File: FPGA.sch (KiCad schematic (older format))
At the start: 14 parts, among them U13 ADS1015, U14 SiT8008B, U8 GW1N-9LQ100

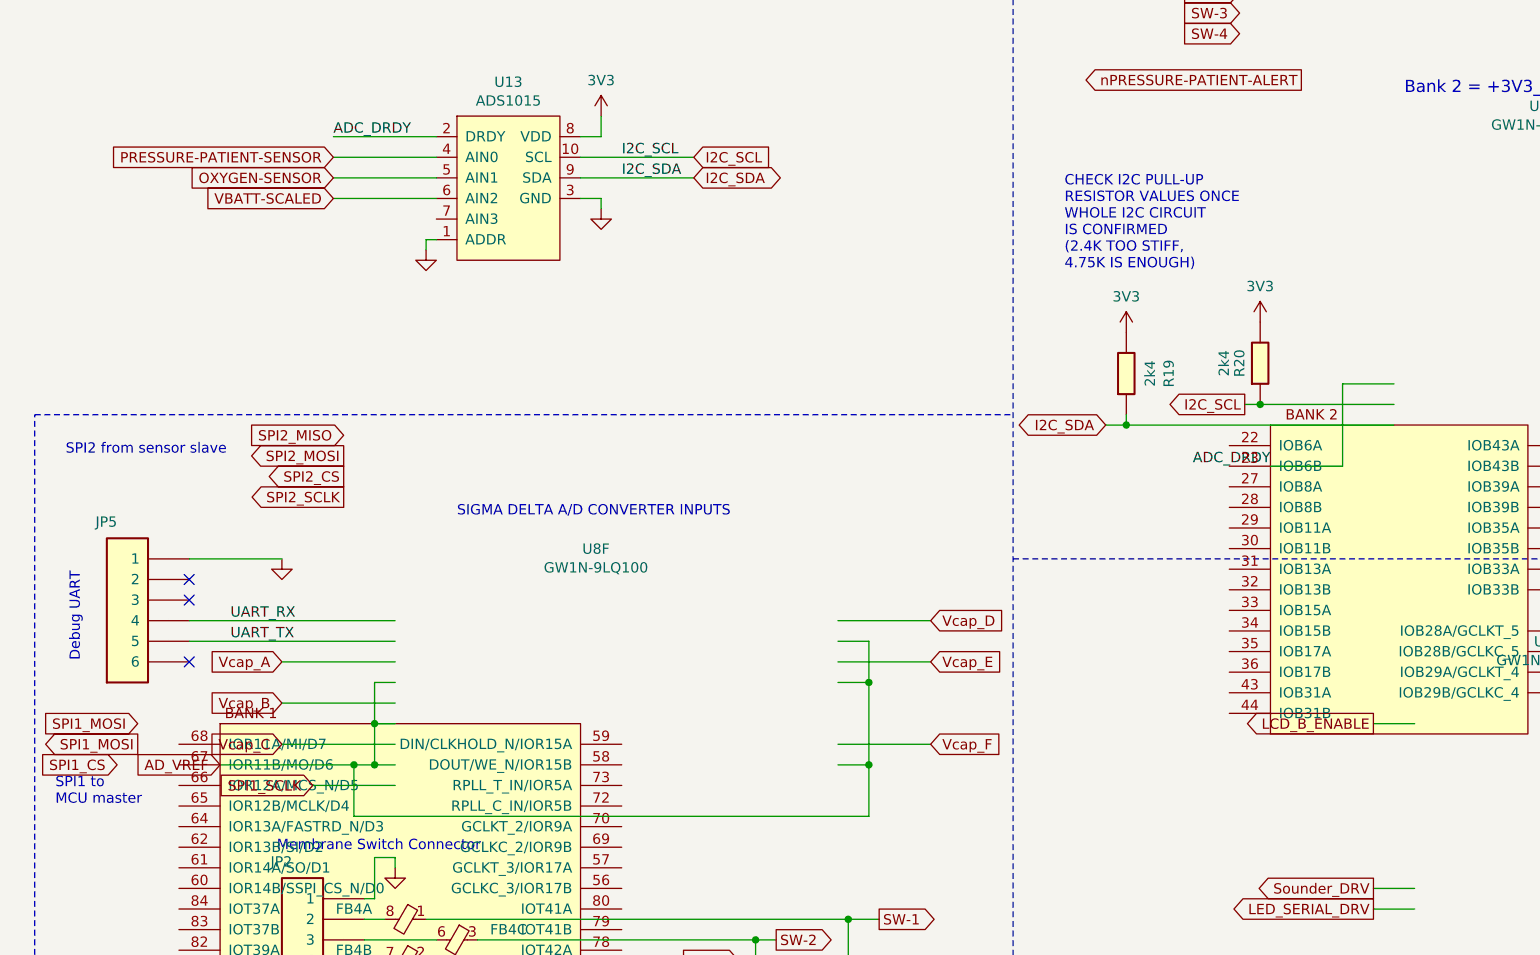
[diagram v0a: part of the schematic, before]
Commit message: SPI from FPGA to MCU and pressure sensor pins changed
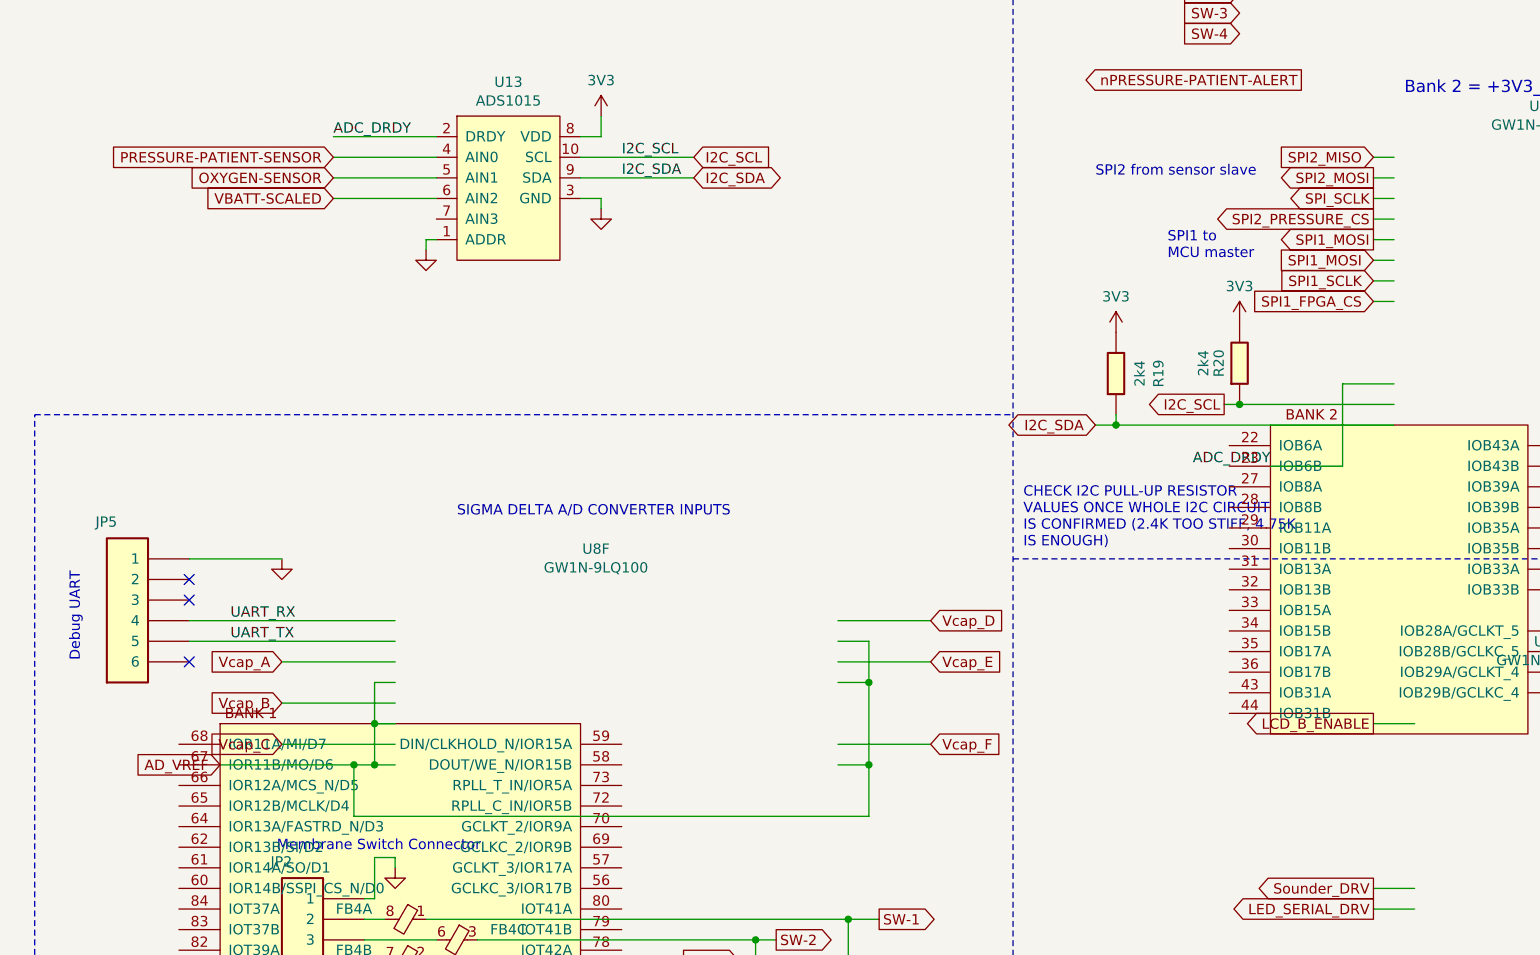
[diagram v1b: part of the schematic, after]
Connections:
- net labels added: SPI1_FPGA_CS, SPI2_PRESSURE_CS, SPI_SCLK
- net labels removed: SPI1_CS, SPI2_CS, SPI2_SCLK
- wire segments 105 -> 112
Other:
- note added: "CHECK I2C PULL-UP RESISTOR\nVALUES ONCE WHOLE I2C CIRCUIT\nIS CONFIRMED (2.4K TOO STIFF, 4.75K\nIS ENOUGH)"
- note removed: "CHECK I2C PULL-UP\nRESISTOR VALUES ONCE\nWHOLE I2C CIRCUIT\nIS CONFIRMED\n(2.4K TOO STIFF,\n4.75K IS ENOUGH)"
- moved on the sheet: R19, R20
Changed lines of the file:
@@
 L OpenVent:2k4_0603_Chip_Resistor,_1%,_0.1W R19
 U 1 1 5FD4D09C
-P 5700 2650
-F 0 "R19" H 5800 2343 50  0000 C CNN
-F 1 "2k4_0603_Chip_Resistor,_1%,_0.1W" H 5700 2650 50  0001 C CNN
-F 2 "Resistor_SMD:R_0603_1608Metric" H 5700 2650 50  0001 C CNN
-F 3 "" H 5700 2650 50  0001 C CNN
-F 4 "2k4" H 5800 2434 50  0000 C CNN "Val"
-F 5 "1%" H 5700 2650 50  0001 C CNN "Tolerance"
-F 6 "0.1W" H 5700 2650 50  0001 C CNN "Watt"
-	1    5700 2650
+P 5650 2650
+F 0 "R19" H 5750 2343 50  0000 C CNN
+F 1 "2k4_0603_Chip_Resistor,_1%,_0.1W" H 5650 2650 50  0001 C CNN
+F 2 "Resistor_SMD:R_0603_1608Metric" H 5650 2650 50  0001 C CNN
+F 3 "" H 5650 2650 50  0001 C CNN
+F 4 "2k4" H 5750 2434 50  0000 C CNN "Val"
+F 5 "1%" H 5650 2650 50  0001 C CNN "Tolerance"
+F 6 "0.1W" H 5650 2650 50  0001 C CNN "Watt"
+	1    5650 2650
 	0    -1   -1   0
 $EndComp
@@
 L OpenVent:2k4_0603_Chip_Resistor,_1%,_0.1W R20
 U 1 1 5FD4E271
-P 6350 2600
-F 0 "R20" H 6450 2600 50  0000 C CNN
-F 1 "2k4_0603_Chip_Resistor,_1%,_0.1W" H 6350 2600 50  0001 C CNN
-F 2 "Resistor_SMD:R_0603_1608Metric" H 6350 2600 50  0001 C CNN
-F 3 "" H 6350 2600 50  0001 C CNN
-F 4 "2k4" H 6450 2675 50  0000 C CNN "Val"
-F 5 "1%" H 6350 2600 50  0001 C CNN "Tolerance"
-F 6 "0.1W" H 6350 2600 50  0001 C CNN "Watt"
-	1    6350 2600
+P 6250 2600
+F 0 "R20" H 6350 2600 50  0000 C CNN
+F 1 "2k4_0603_Chip_Resistor,_1%,_0.1W" H 6250 2600 50  0001 C CNN
+F 2 "Resistor_SMD:R_0603_1608Metric" H 6250 2600 50  0001 C CNN
+F 3 "" H 6250 2600 50  0001 C CNN
+F 4 "2k4" H 6350 2675 50  0000 C CNN "Val"
+F 5 "1%" H 6250 2600 50  0001 C CNN "Tolerance"
+F 6 "0.1W" H 6250 2600 50  0001 C CNN "Watt"
+	1    6250 2600
 	0    -1   -1   0
 $EndComp
@@
 L OpenVent:3V3 #PWR031
 U 1 1 5FD519F4
-P 5800 2350
-F 0 "#PWR031" H 5800 2200 50  0001 C CNN
-F 1 "3V3" H 5800 2523 50  0000 C CNN
-F 2 "" H 5800 2350 50  0001 C CNN
-F 3 "" H 5800 2350 50  0001 C CNN
-	1    5800 2350
+P 5750 2350
+F 0 "#PWR031" H 5750 2200 50  0001 C CNN
+F 1 "3V3" H 5750 2523 50  0000 C CNN
+F 2 "" H 5750 2350 50  0001 C CNN
+F 3 "" H 5750 2350 50  0001 C CNN
+	1    5750 2350
 	1    0    0    -1
 $EndComp
@@
 Wire Notes Line
 	500  7750 500  2750
-Text Notes 5500 2050 0    50   ~ 0
-CHECK I2C PULL-UP\nRESISTOR VALUES ONCE\nWHOLE I2C CIRCUIT\nIS CONFIRMED\n(2.4K TOO STIFF,\n4.75K IS ENOUGH)
-Text GLabel 6375 2700 0    50   Output ~ 0
+Text Notes 5300 3400 0    50   ~ 0
+CHECK I2C PULL-UP RESISTOR\nVALUES ONCE WHOLE I2C CIRCUIT\nIS CONFIRMED (2.4K TOO STIFF, 4.75K\nIS ENOUGH)
+Text GLabel 6275 2700 0    50   Output ~ 0
 I2C_SCL
-Text GLabel 5700 2800 0    50   BiDi ~ 0
+Text GLabel 5650 2800 0    50   BiDi ~ 0
 I2C_SDA
 Text GLabel 3700 1500 2    50   Input ~ 0
@@
 I2C_SDA
 Wire Wire Line
-	6375 2700 6450 2700
+	6275 2700 6350 2700
 $Comp
 L OpenVent:3V3 #PWR066
 U 1 1 602573F8
-P 6450 2300
-F 0 "#PWR066" H 6450 2150 50  0001 C CNN
-F 1 "3V3" H 6450 2473 50  0000 C CNN
-F 2 "" H 6450 2300 50  0001 C CNN
-F 3 "" H 6450 2300 50  0001 C CNN
-	1    6450 2300
+P 6350 2300
+F 0 "#PWR066" H 6350 2150 50  0001 C CNN
+F 1 "3V3" H 6350 2473 50  0000 C CNN
+F 2 "" H 6350 2300 50  0001 C CNN
+F 3 "" H 6350 2300 50  0001 C CNN
+	1    6350 2300
 	1    0    0    -1
 $EndComp
@@
 Text Notes 2550 3250 0    50   ~ 0
 SIGMA DELTA A/D CONVERTER INPUTS
-Wire Wire Line
-	7100 2700 6450 2700
-Connection ~ 6450 2700
-Wire Wire Line
-	5700 2800 5800 2800
-Wire Wire Line
-	5800 2750 5800 2800
-Connection ~ 5800 2800
-Wire Wire Line
-	5800 2800 7100 2800
+Connection ~ 6350 2700
 Wire Wire Line
 	9000 2400 9000 3000
@@
 Wire Notes Line
 	500  2750 5250 2750
-Text GLabel 1850 4550 0    50   Input ~ 0
+Text GLabel 7000 2100 0    50   Input ~ 0
 SPI1_SCLK
-Wire Wire Line
-	1850 4550 2250 4550
-Text GLabel 900  4450 0    50   Input ~ 0
-SPI1_CS
-Text GLabel 1000 4250 0    50   Input ~ 0
+Text GLabel 7000 2200 0    50   Input ~ 0
+SPI1_FPGA_CS
+Text GLabel 7000 2000 0    50   Input ~ 0
 SPI1_MOSI
-Text GLabel 1000 4350 0    50   Output ~ 0
+Text GLabel 7000 1900 0    50   Output ~ 0
 SPI1_MOSI
 Wire Wire Line
@@
 Wire Wire Line
 	4550 4450 4550 4700
-Text GLabel 2000 2950 0    50   Output ~ 0
+Text GLabel 7000 1600 0    50   Output ~ 0
 SPI2_MOSI
-Text GLabel 2000 2850 0    50   Input ~ 0
+Text GLabel 7000 1500 0    50   Input ~ 0
 SPI2_MISO
-Text GLabel 2000 3050 0    50   Output ~ 0
-SPI2_CS
-Text GLabel 2000 3150 0    50   Output ~ 0
-SPI2_SCLK
-Text Notes 600  4650 0    50   ~ 0
+Text GLabel 7000 1800 0    50   Output ~ 0
+SPI2_PRESSURE_CS
+Text GLabel 7000 1700 0    50   Output ~ 0
+SPI_SCLK
+Text Notes 6000 2000 0    50   ~ 0
 SPI1 to\nMCU master
-Text Notes 650  2950 0    50   ~ 0
+Text Notes 5650 1600 0    50   ~ 0
 SPI2 from sensor slave
+Wire Wire Line
+	5750 2750 5750 2800
+Connection ~ 5750 2800
+Wire Wire Line
+	5750 2800 5650 2800
+Wire Wire Line
+	7100 1500 7000 1500
+Wire Wire Line
+	7100 1600 7000 1600
+Wire Wire Line
+	7100 1800 7000 1800
+Wire Wire Line
+	7000 1700 7100 1700
+Wire Wire Line
+	6350 2700 7100 2700
+Wire Wire Line
+	5750 2800 7100 2800
+Wire Wire Line
+	7100 1900 7000 1900
+Wire Wire Line
+	7100 2000 7000 2000
+Wire Wire Line
+	7100 2100 7000 2100
+Wire Wire Line
+	7100 2200 7000 2200
 $EndSCHEMATC

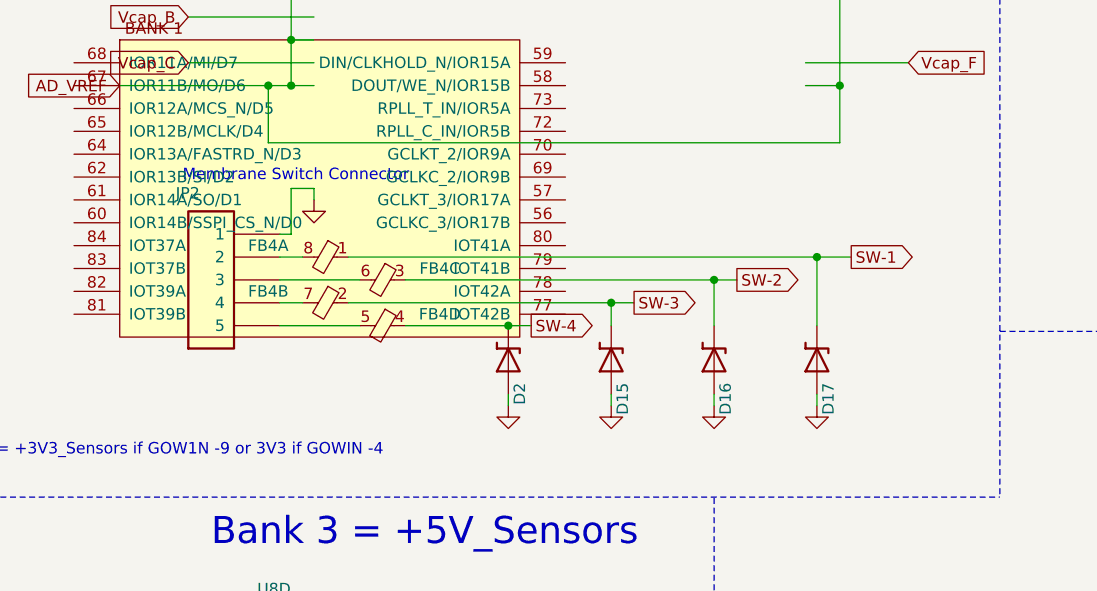
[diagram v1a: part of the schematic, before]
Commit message: Push buttons moved from FPGA pg 6 to UI pg 8
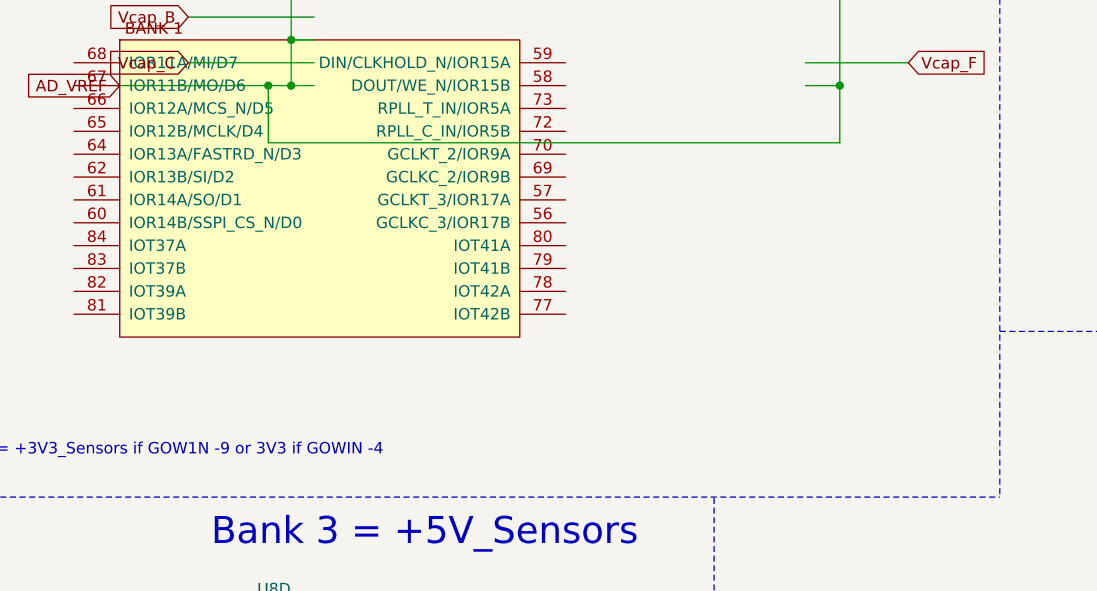
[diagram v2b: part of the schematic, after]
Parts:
- removed D15, D16, D17, D2: SP3522-01UTG, 0603 diode, symbol OpenVent:SP3522-01UTG
- removed FB4: BLA31BD121SN4D, F_Inductors:Murata_BLA31, symbol OpenVent:BLA31BD121SN4D
- removed JP2: Pin_Header,_1x5-Way,_2.54mm_Pitch, Connector_PinHeader_2.54mm:PinHeader_1x05_P2.54mm_Vertical, symbol OpenVent:Pin_Header,_1x5-Way,_2.54mm_Pitch
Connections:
- wire segments 112 -> 89
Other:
- note removed: "Membrane Switch Connector"

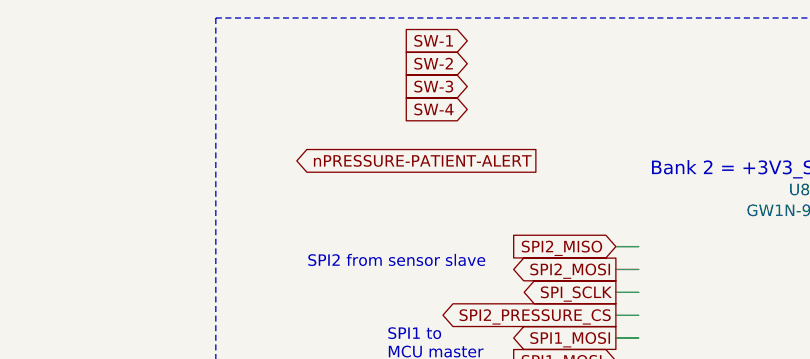
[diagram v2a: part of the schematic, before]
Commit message: Push button signals SW-1 to SW-4 renamed with functional names, PB_MUTE etc
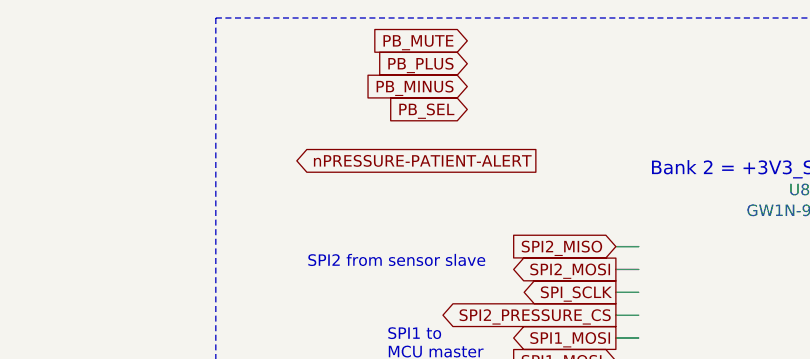
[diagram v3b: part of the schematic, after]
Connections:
- net labels added: PB_MINUS, PB_MUTE, PB_PLUS, PB_SEL
- net labels removed: SW-1, SW-2, SW-3, SW-4
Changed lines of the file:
@@
 Motor_off
 Text GLabel 6350 600  0    50   Input ~ 0
-SW-1
+PB_MUTE
 Text GLabel 6350 700  0    50   Input ~ 0
-SW-2
+PB_PLUS
 Text GLabel 6350 800  0    50   Input ~ 0
-SW-3
+PB_MINUS
 Text GLabel 6350 900  0    50   Input ~ 0
-SW-4
+PB_SEL
 Text GLabel 9550 1500 2    50   Output ~ 0
 Vref_DRV
